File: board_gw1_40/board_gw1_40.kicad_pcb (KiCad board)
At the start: 4 copper layers, 50 x 15.2 mm, 213 parts, among them J1 USB_C_Receptacle, Q1 2N7002, Q10 2N7002, Q11 2N7002, Q12 2N7002, Q13 2N7002, Q14 2N7002, Q15 2N7002, Q16 2N7002, Q17 2N7002, Q18 2N7002, Q19 2N7002, Q2 2N7002, Q20 2N7002, Q21 2N7002, Q22 2N7002, Q23 2N7002, Q24 2N7002, Q25 2N7002, Q27 2N7002, Q28 2N7002, Q29 2N7002, Q3 2N7002, Q30 2N7002, Q31 2N7002, Q32 2N7002, Q33 2N7002, Q34 2N7002, Q35 2N7002, Q36 2N7002, Q37 2N7002, Q38 2N7002, Q39 2N7002, Q4 2N7002, Q40 2N7002, Q41 2N7002, Q5 2N7002, Q6 2N7002, Q7 2N7002, Q8 2N7002, Q9 2N7002, U1 GW1NR-LV9-QN88-C6/I5, U11 FT232H, U2 ESD224DQA, U3 MIC5203-3.3BM5, U4 APS6404L-3SQR-ZR, U5 MIC5504-1.2YM5, U6 TPS562242, U7 W25Q16JVUXIQ, X2 27MHz, Y1 12MHz

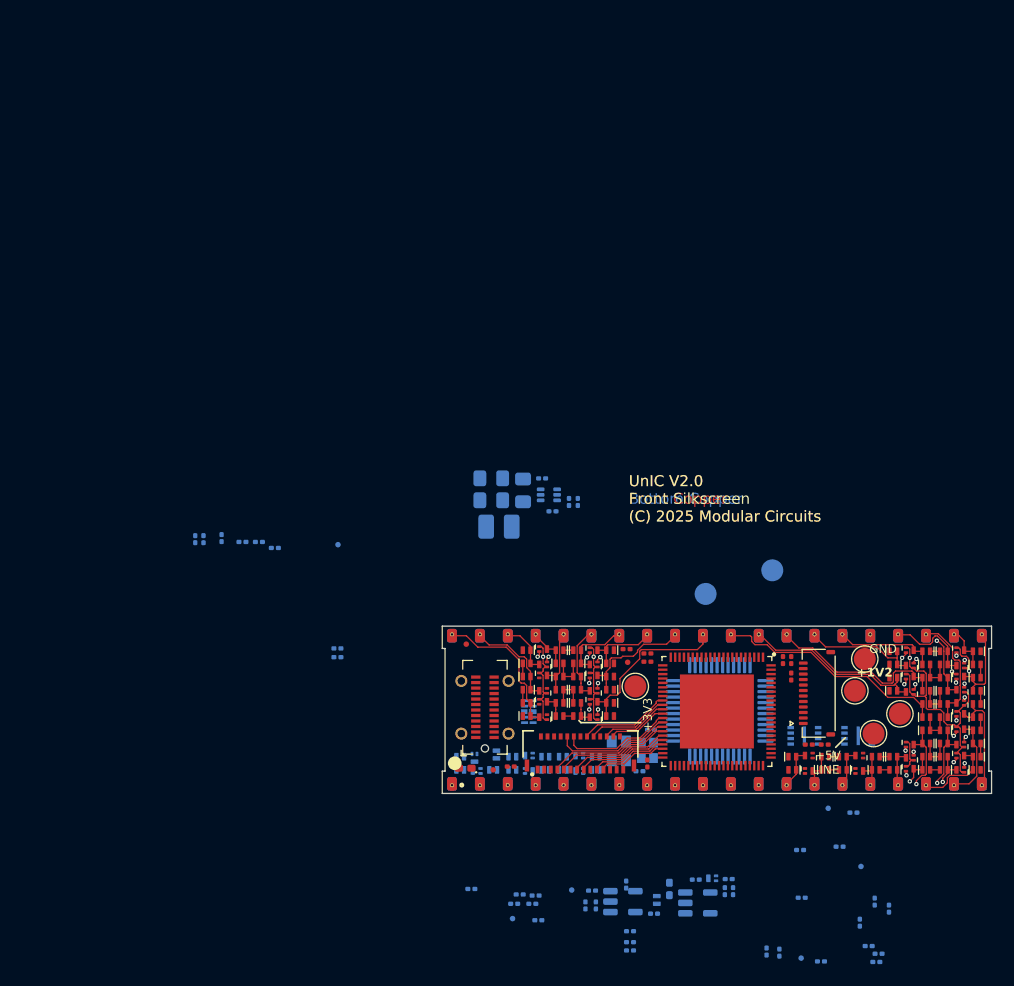
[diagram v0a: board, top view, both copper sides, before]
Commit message: Some progress with 40-pin board.
In the end, it might not be any better than the old one.
We shall see...
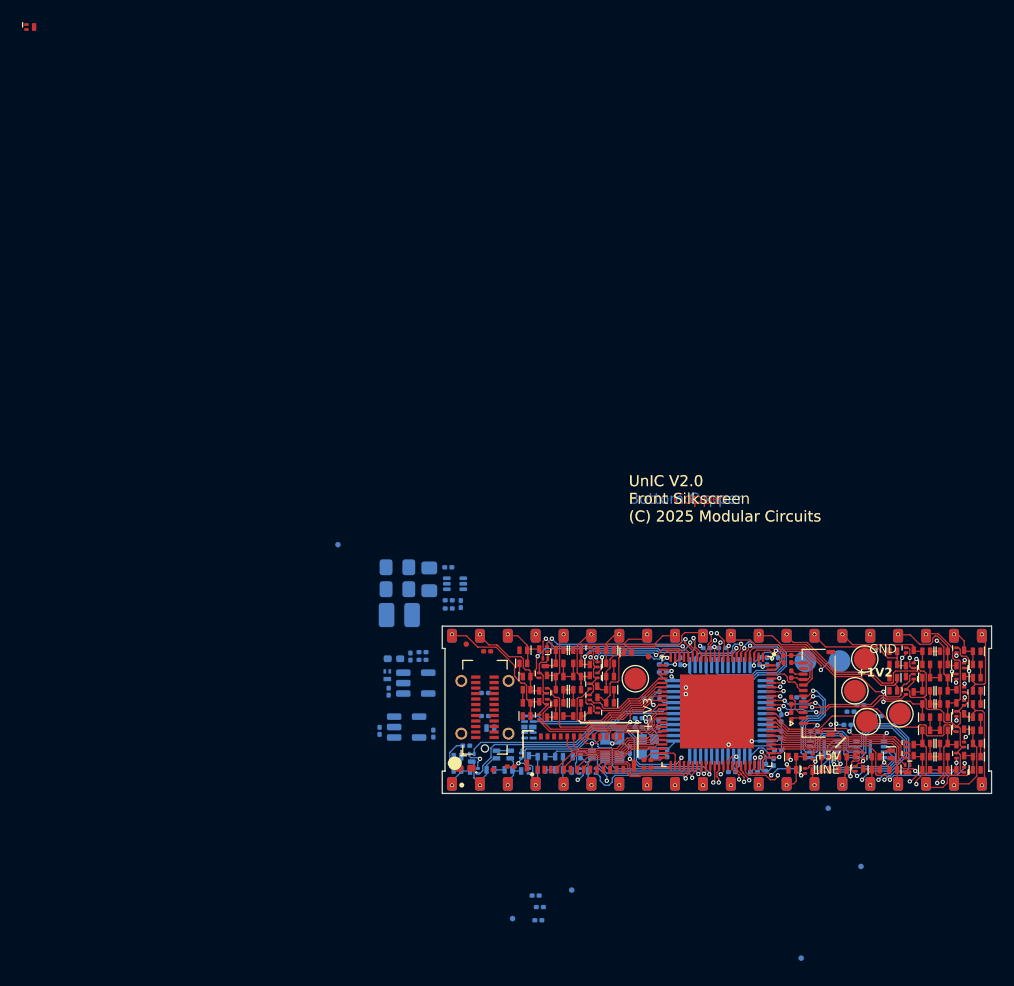
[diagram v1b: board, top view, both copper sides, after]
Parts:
- added Q26: 2N7002, UNIC:SOT-883, F.Cu at (0.76, 0.51)
- C18, R3: moved to F.Cu
- C20, C23, C4: moved to B.Cu
- moved R23 44.1 mm to (57.3, 64.0)
- moved C27 43.6 mm to (56.2, 63.5), turned to 180 degrees
- moved R21 43.2 mm to (58.0, 64.0), turned to 90 degrees
- moved C26 41.2 mm to (69.2, 65.0), turned to -90 degrees
- moved R22 40.8 mm to (69.2, 63.5), turned to 90 degrees
- moved R24 40.5 mm to (58.1, 61.4), turned to 90 degrees
- moved C28 38.7 mm to (58.4, 59.3)
- moved R6 38.4 mm to (60.0, 58.3), turned to 90 degrees
- moved R12 37.8 mm to (40.5, 66.0), turned to 0 degrees
- moved C3 35.7 mm to (36.5, 57.5), turned to 180 degrees
- moved R15 35.4 mm to (35.4, 57.9), turned to 90 degrees
- moved R3 35.3 mm to (69.4, 58.1), turned to -90 degrees
- moved Q41 34.9 mm to (33.3, 59.5), turned to -90 degrees
- moved R14 34.7 mm to (36.5, 58.1), turned to 180 degrees
- moved R17 32.8 mm to (33.4, 61.0), turned to 90 degrees
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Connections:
- net Net-(U1-IOR13A/FASTRD_N/D3) renamed /MODE1
- J_EXT1 pad 19: /IO5A -> /IO5B
- J_EXT1 pad 21: /IO5B -> /IO5A
- R2 pad 2: /LCD_RST_N -> /LCD_CS_N
- R3 pad 1: /LCD_RST_N -> /LCD_CS_N
- U1 pad 11: /PIN28_F -> unconnected-(U1-IOL15A/GCLKT_6-Pad11)
- U1 pad 13: /PIN33_F -> /PIN20_F
- U1 pad 14: /PIN34_F -> unconnected-(U1-IOL22B-Pad14)
- U1 pad 15: /PIN35_F -> /PIN33_F
- U1 pad 17: /PIN39_F -> /PIN38_F
- U1 pad 18: /PIN38_F -> /PIN37_F
- U1 pad 19: /PIN40_F -> /PIN34_F
- U1 pad 20: /PIN37_F -> /PIN35_F
- U1 pad 25: /PIN6_F -> /PIN12_F
- U1 pad 26: /PIN5_F -> /PIN31_F
- U1 pad 27: /PIN3_F -> /PIN7_F
- U1 pad 28: /PIN4_F -> /PIN32_F
- U1 pad 29: /PIN1_F -> /PIN39_F
- U1 pad 30: /PIN2_F -> /PIN40_F
- U1 pad 31: /IO4A -> /PIN8_F
- U1 pad 32: /IO4B -> /PIN2_F
- U1 pad 33: /IO6A -> /IO4A
- U1 pad 34: /IO6B -> /IO4B
- U1 pad 35: /IO2B -> /IO6A
- U1 pad 36: /IO2A -> /IO6B
- U1 pad 37: /IO1A -> /IO2B
- U1 pad 38: /IO1B -> /IO2A
- U1 pad 39: /IO3A -> /IO1A
- U1 pad 40: /IO3B -> /IO1B
- U1 pad 41: /IO5A -> /IO3A
- U1 pad 42: /IO5B -> /IO3B
- U1 pad 47: /PIN7_F -> /PIN1_F
- U1 pad 48: /PIN8_F -> /IO5B
- U1 pad 49: /PIN19_F -> /IO5A
- U1 pad 50: /PIN12_F -> /PIN6_F
- U1 pad 51: /PIN18_F -> /PIN5_F
- U1 pad 53: /PIN17_F -> /PIN3_F
- U1 pad 54: /PIN16_F -> /PIN4_F
- U1 pad 68: /PIN15_F -> /PIN13_F
- U1 pad 69: /PIN10_F -> /PIN16_F
- U1 pad 70: /PIN9_F -> /PIN15_F
- U1 pad 71: /PIN20_F -> /PIN11_F
- U1 pad 72: /PIN13_F -> /PIN18_F
- U1 pad 73: /PIN11_F -> /PIN17_F
- U1 pad 74: /PIN30_F -> /PIN9_F
- U1 pad 75: /PIN21_F -> /PIN10_F
- U1 pad 77: /PIN22_F -> /PIN19_F
- U1 pad 79: /LCD_CS_N -> /PIN28_F
- U1 pad 80: /PIN23_F -> /PIN29_F
- U1 pad 81: /PIN29_F -> /PIN23_F
- U1 pad 84: /PIN32_F -> unconnected-(U1-IOT10A-Pad84)
- U1 pad 86: /PIN31_F -> /LCD_RST_N
- U1 pad 87: /LCD_RST_N -> /LCD_CS_N
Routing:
- net /SPI_IO3: track 0.00 -> 46.5 mm, vias 0 -> 3
- net GND: track 18.3 -> 63.7 mm, vias 0 -> 17
- net /SPI_CLK: track 0.00 -> 43.6 mm, vias 0 -> 3
- net /SPI_MOSI_IO0: track 0.00 -> 41.8 mm, vias 0 -> 3
- net +3V3: track 0.00 -> 32.4 mm, vias 0 -> 12
- net /MODE1: track 0.00 -> 31.1 mm, vias 0 -> 2
- net /PIN1_F: track 0.00 -> 24.7 mm, vias 0 -> 1
- net /SPI_IO2: track 0.00 -> 23.5 mm, vias 0 -> 2
- net /SPI_MISO_IO1: track 0.00 -> 23.0 mm, vias 0 -> 2
- net /PIN3_F: track 0.00 -> 22.6 mm, vias 0 -> 1
- net /PIN4_F: track 0.00 -> 22.0 mm, vias 0 -> 1
- net /PIN11_F: track 0.40 -> 21.6 mm, vias 1 -> 2
- net /PIN19_F: track 0.48 -> 21.3 mm, vias 1 -> 0
- net /PIN18_F: track 0.48 -> 20.2 mm, vias 1 -> 2
- net /PIN2_F: track 0.00 -> 19.6 mm, vias 0 -> 1
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
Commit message: Some progress on 40-pin USB
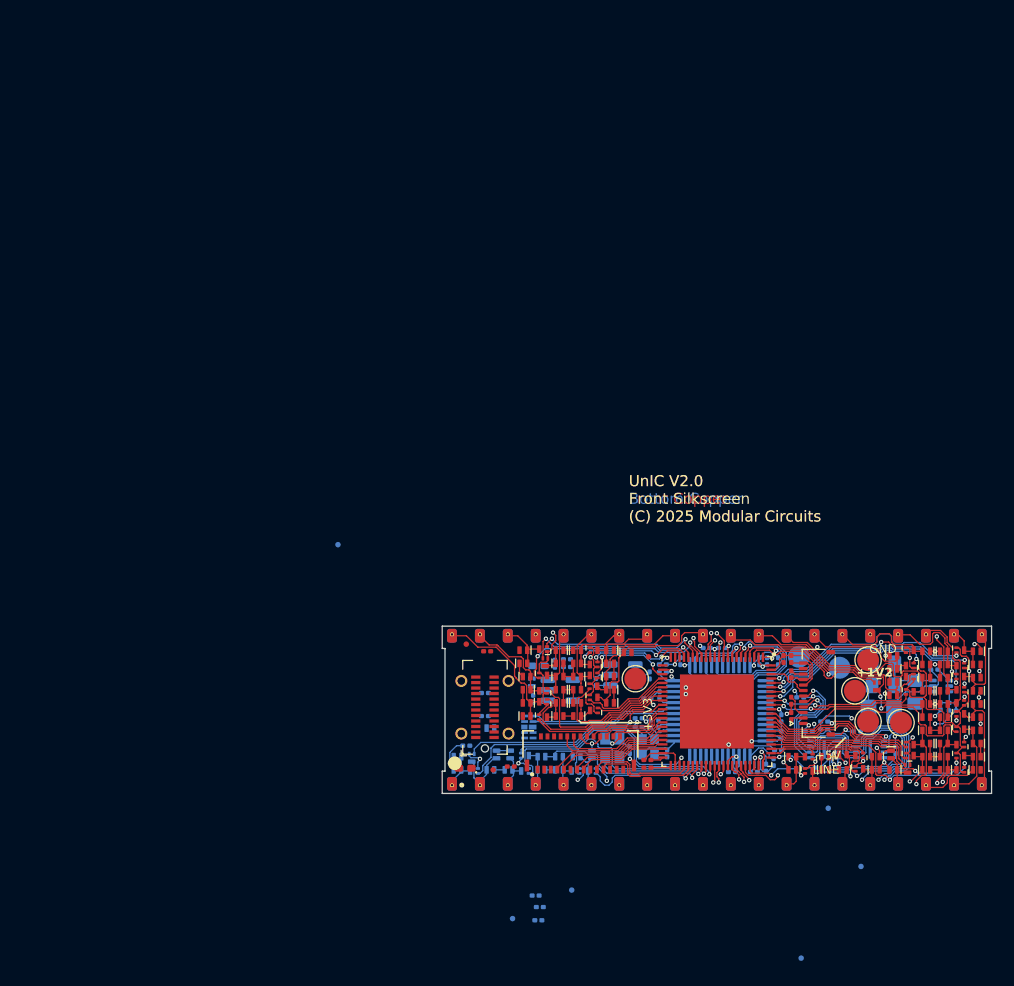
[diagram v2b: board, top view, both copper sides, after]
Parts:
- moved Q26 97.7 mm to (77.9, 60.6), turned to -90 degrees
- moved R4 46.8 mm to (84.8, 62.1), turned to 180 degrees
- moved C32 46.8 mm to (84.8, 62.8), turned to 180 degrees
- moved C7 45.6 mm to (78.5, 60.5)
- moved C5 45.4 mm to (81.4, 61.1)
- moved C6 45.2 mm to (83.1, 59.0)
- moved U6 45.2 mm to (83.7, 60.5)
- moved C8 44.8 mm to (78.5, 58.5)
- moved L1 44.8 mm to (78.3, 62.9)
- moved R5 44.7 mm to (83.7, 62.4)
- moved C2 20.4 mm to (57.2, 59.6), turned to -90 degrees
- moved U5 20.3 mm to (54.7, 59.5)
- moved C10 20.2 mm to (52.3, 60.2)
- moved C3 13.2 mm to (49.6, 58.1)
- moved Q41 13.2 mm to (46.4, 60.2)
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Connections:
- U1 pad 11: unconnected-(U1-IOL15A/GCLKT_6-Pad11) -> /PIN23_F
- U1 pad 14: unconnected-(U1-IOL22B-Pad14) -> /PIN12_F
- U1 pad 15: /PIN33_F -> /PIN25_F
- U1 pad 19: /PIN34_F -> /PIN33_F
- U1 pad 20: /PIN35_F -> /PIN34_F
- U1 pad 25: /PIN12_F -> /PIN35_F
- U1 pad 3: /PIN27_F -> /PIN30_F
- U1 pad 81: /PIN23_F -> /PIN27_F
- U1 pad 82: /PIN24_F -> /PIN21_F
- U1 pad 83: /PIN25_F -> /PIN24_F
- U1 pad 84: unconnected-(U1-IOT10A-Pad84) -> /PIN26_F
- U1 pad 85: /PIN26_F -> /PIN22_F
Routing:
- net /PIN12_F: track 0.54 -> 38.7 mm, vias 1 -> 2
- net /PIN25_F: track 1.20 -> 32.7 mm
- net /PIN23_F: track 1.14 -> 30.3 mm
- net /PIN20_F: track 11.1 -> 36.6 mm
- net /PIN21_F: track 0.34 -> 21.5 mm, vias 1 -> 2
- net /PIN22_F: track 0.28 -> 20.4 mm, vias 1 -> 2
- net /PIN24_F: track 1.45 -> 20.4 mm
- net +3V3: track 32.4 -> 49.9 mm, vias 12 -> 14
- net /PIN30_F: track 0.00 -> 13.6 mm
- net /PIN26_F: track 1.38 -> 14.5 mm
- net unconnected-(U1-IOL22B-Pad14): track 12.0 -> 0.00 mm, vias 1 -> 0
- net GND: track 63.7 -> 75.6 mm, vias 17 -> 24
- net unconnected-(U1-IOL15A/GCLKT_6-Pad11): track 9.36 -> 0.00 mm, vias 1 -> 0
- net /PIN27_F: track 7.04 -> 16.4 mm, vias 1 -> 2
- net Net-(U6-SW): track 0.00 -> 7.15 mm
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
